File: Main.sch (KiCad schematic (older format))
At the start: 41 parts, among them J1 USB_A FEMALE, J2 USB_A MALE, SW1 SW_Push, SW2 SW_Push, SW3 SW_Push, U1 LTC6995-1, U2 MSP430F5529IPN, U3 TPS2557, U4 TPS2557, U5 TPS2557, U6 TPS2557

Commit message: Addded first portion of battery heater. Contains the temperature sensor and resistive heater. Need to add logic if it will be driven by OBC.
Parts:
- CC1, CC2, CC3, CC4: symbol 2019-06-26_20-23-01:LTC2942CDCB-TRMPBF -> Main-rescue:LTC2942CDCB-TRMPBF-2019-06-26_20-23-01
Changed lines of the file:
@@
 EESchema Schematic File Version 4
 LIBS:Main-cache
-EELAYER 29 0
+EELAYER 26 0
 EELAYER END
 $Descr A2 23386 16535
 encoding utf-8
-Sheet 1 36
+Sheet 1 37
 Title "Electrical Power System"
 Date "2019-04-25"
@@
 	6450 3250 6450 3650
 $Comp
-L 2019-06-26_20-23-01:LTC2942CDCB-TRMPBF CC1
+L Main-rescue:LTC2942CDCB-TRMPBF-2019-06-26_20-23-01 CC1
 U 1 1 5D1F267D
 P 9300 5950
@@
 $EndComp
 $Comp
-L 2019-06-26_20-23-01:LTC2942CDCB-TRMPBF CC2
+L Main-rescue:LTC2942CDCB-TRMPBF-2019-06-26_20-23-01 CC2
 U 1 1 5D20202F
 P 9300 7050
@@
 $EndComp
 $Comp
-L 2019-06-26_20-23-01:LTC2942CDCB-TRMPBF CC3
+L Main-rescue:LTC2942CDCB-TRMPBF-2019-06-26_20-23-01 CC3
 U 1 1 5D20BC4B
 P 9300 8200
@@
 $EndComp
 $Comp
-L 2019-06-26_20-23-01:LTC2942CDCB-TRMPBF CC4
+L Main-rescue:LTC2942CDCB-TRMPBF-2019-06-26_20-23-01 CC4
 U 1 1 5D2149C4
 P 9300 9400
@@
 Text GLabel 11300 9700 2    43   Input ~ 0
 MSP_46_SDA
+$Sheet
+S 8900 12600 500  150
+U 5D20C8DB
+F0 "Battery Heater" 50
+F1 "batteryHeater.sch" 50
+$EndSheet
 $EndSCHEMATC

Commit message: Revisions to battery charge and discharge control. SPV1040 now regulates to 4.2V.
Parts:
- removed CC1, CC2, CC3, CC4: LTC2942, DFN-6_DCB, symbol Main-rescue:LTC2942CDCB-TRMPBF-2019-06-26_20-23-01
- removed J1: USB_A FEMALE, symbol Main-rescue:USB_A-Connector
- removed J2: USB_A MALE, symbol Main-rescue:Conn_01x02-Connector_Generic
- removed PS1: HS-40012, Converter_ACDC:Converter_ACDC_Hahn_HS-400xx_THT, symbol Main-rescue:HS-40012-Converter_ACDC
- removed R1: TBD, symbol Main-rescue:R_Shunt-Device
- removed TH1: 10k, symbol Main-rescue:Thermistor_NTC-Device
- added C? (x2): 0.22u, symbol Device:C
- added C? (x2): 0.1u, symbol Device:C
- added C?: 10u, symbol Device:C
- added D? (x2): D_Schottky, symbol Device:D_Schottky
- added R?: 10m, symbol Main-rescue:R-Device
- added R? (x2): 100k, symbol Device:R
- added R? (x2): R, symbol Device:R
- added U? (x2): TPS2557, symbol Main-rescue:TPS2557
- added U?: LTC2942, symbol Main-rescue:LTC2942
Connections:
- net GNDD: now also C?.2, C?.2, C?.2, C?.2, C?.2, R?.2, R?.2, U?.1 (GND), U?.1 (GND), U?.2 (GND)
- net BDR/5V renamed MPB
- net MPB: now also C?.1, D?.1 (K), U?.2 (IN), U?.3 (IN)
- net Cell1/Cell- renamed PACK+
- net PACK+: now also C?.1, D?.1 (K), R?.1, U?.1 (SENSE+), U?.2 (IN), U?.3 (IN)
- new net: C?.1, R?.1, U?.4 (EN), U?.8 (FAULT!)
- new net: R?.1, U?.5 (ILIM) (x2)
- new net: C?.1, D?.2 (A), D?.2 (A), U?.6 (OUT), U?.6 (OUT), U?.7 (OUT), U?.7 (OUT)
- new net: C?.1, R?.2, U?.4 (EN), U?.8 (FAULT!)
- new net AL!CC: U?.5 (AL!/CC)
- new net Cell1/Cell+: R?.2, U?.6 (SENSE-)
- new net ChargeEnable: R?.1
- new net DischargeEnable: R?.2
- new net SCL: U?.3 (SCL)
- new net SDA: U?.4 (SDA)
- no-connect marks 12 -> 10
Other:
- note added: "Main Power Bus"
- note added: "Rsense = 50mV / Imax\nTake Imax = 5A"
- note added: "to loads"
- note removed: "External Charger"
- note removed: "External Charging Circuit\n"
- note removed: "Thermistor"
- note removed: "This diode prevents the BDR from powering the BCR"
- moved on the sheet: C1, C2, C3, C4, C5, C6, C7, C8, R10, R11, R12, R13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

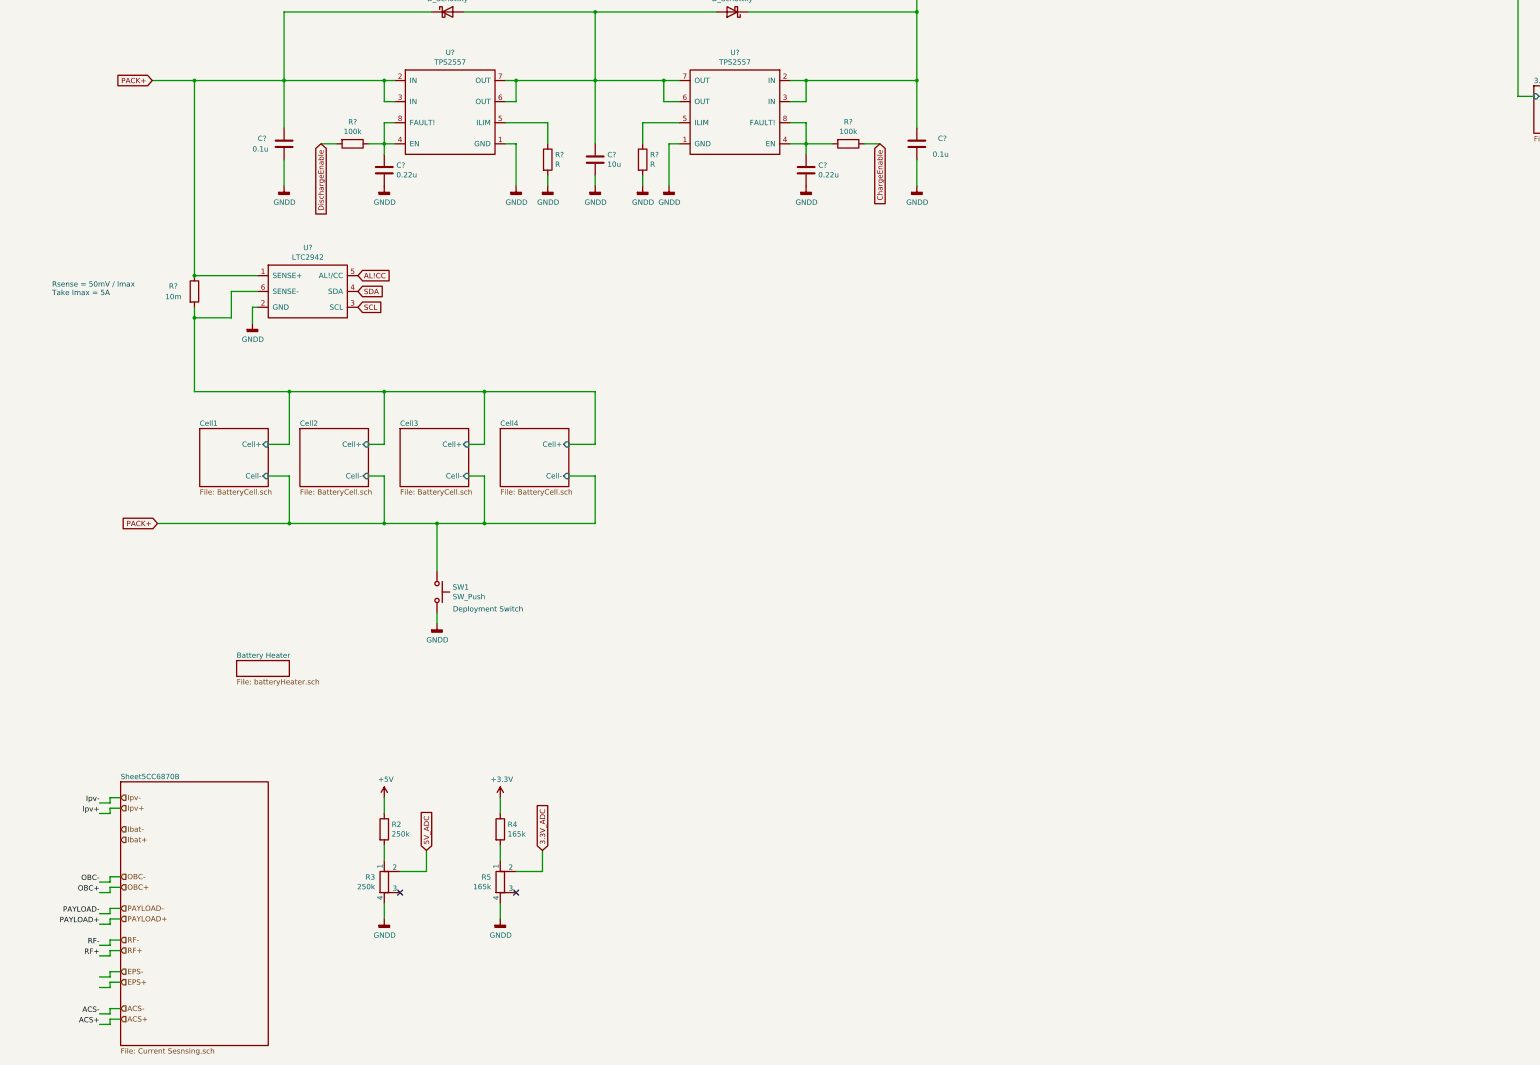
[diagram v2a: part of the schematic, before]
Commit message: Added control circuitry for charge and discharge.
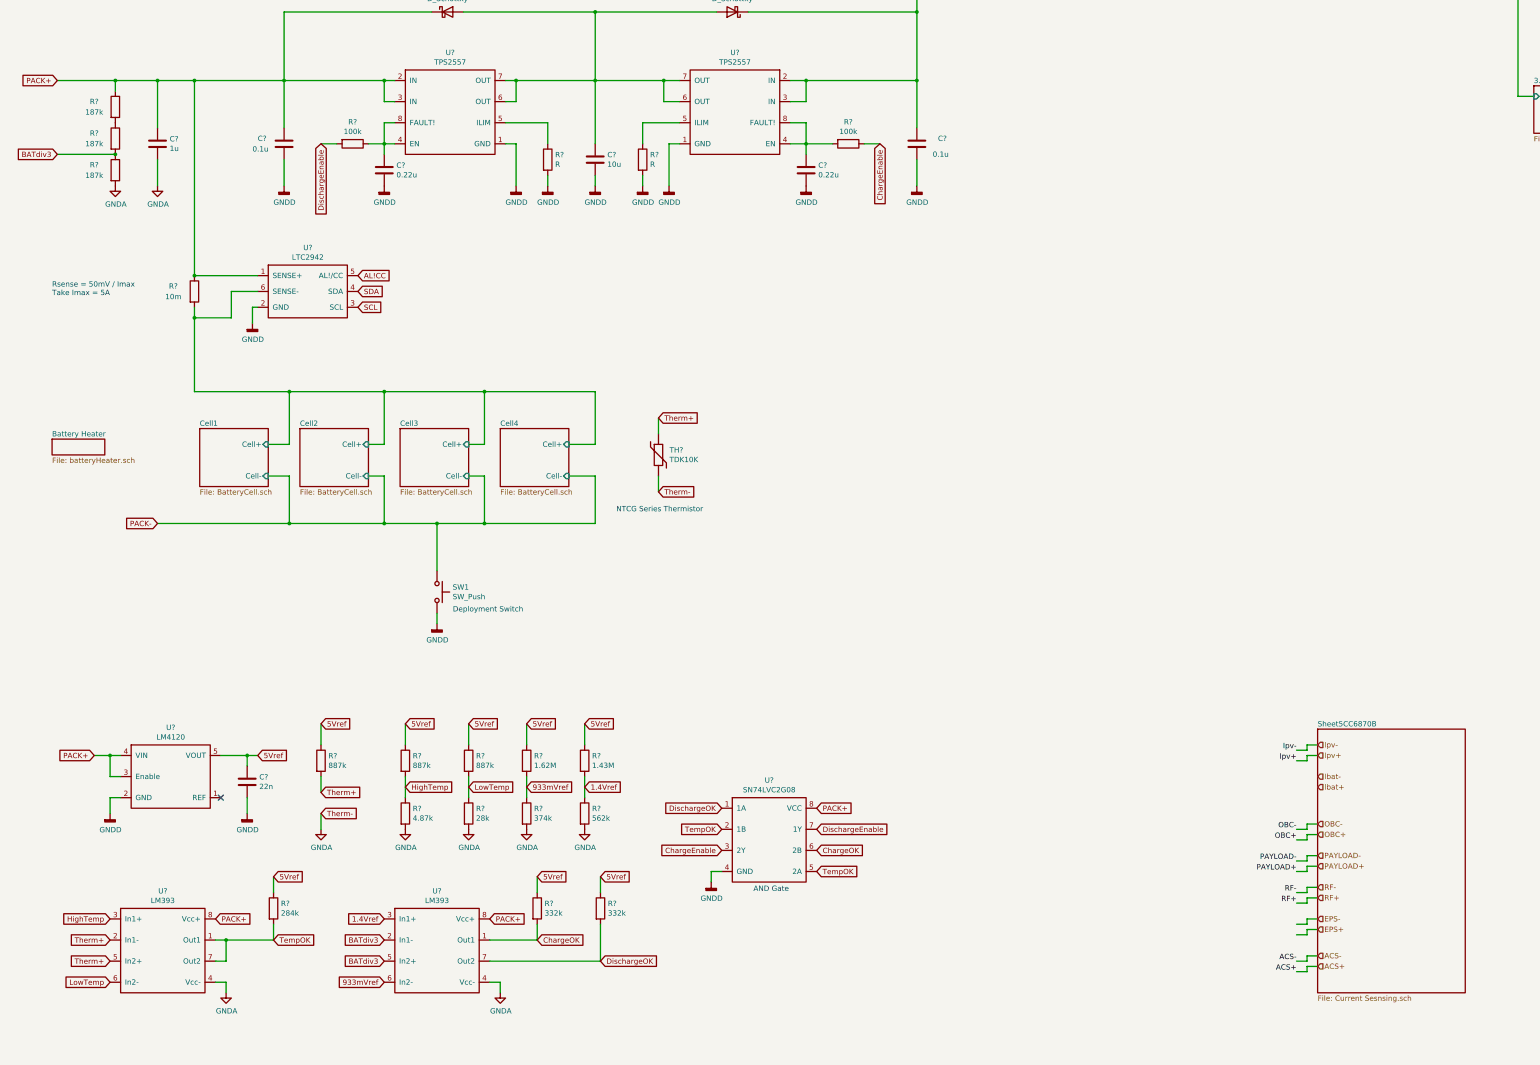
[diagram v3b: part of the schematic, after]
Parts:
- removed R2: 250k, symbol Main-rescue:R-Device
- removed R3: 250k, symbol Main-rescue:R_Shunt-Device
- removed R4: 165k, symbol Main-rescue:R-Device
- removed R5: 165k, symbol Main-rescue:R_Shunt-Device
- added C?: 22n, symbol Device:C
- added C?: 1u, symbol Device:C
- added R? (x3): 887k, symbol Device:R
- added R?: 4.87k, symbol Device:R
- added R?: 28k, symbol Device:R
- added R? (x3): 187k, symbol Main-rescue:R-Device
- added R?: 1.62M, symbol Device:R
- added R?: 374k, symbol Device:R
- added R?: 1.43M, symbol Device:R
- added R?: 562k, symbol Device:R
- added R?: 284k, symbol Device:R
- added R? (x2): 332k, symbol Device:R
- added TH?: TDK10K, symbol Device:Thermistor
- added U?: LM4120, symbol Main-rescue:LM4120
- added U? (x2): LM393, symbol Main-rescue:LM393
- added U?: SN74LVC2G08, symbol Main-rescue:SN74LVC2G08
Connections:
- net ChargeEnable: now also U?.3 (2Y)
- net DischargeEnable: now also U?.7 (1Y)
- net GNDD: now also C?.2, U?.2 (GND), U?.4 (GND)
- net PACK+: now also C?.1, R?.1, U?.3 (Enable), U?.4 (VIN), U?.8 (VCC), U?.8 (Vcc+), U?.8 (Vcc+); no longer SW1.1
- new net: R?.1, R?.2
- new net 1.4Vref: R?.1, R?.2, U?.3 (In1+)
- new net 5Vref: C?.1, R?.1, R?.1, R?.1, R?.1, R?.1, R?.1, R?.1, R?.1, U?.5 (VOUT)
- new net 933mVref: R?.1, R?.2, U?.6 (In2-)
- new net BATdiv3: R?.1, R?.2, U?.2 (In1-), U?.5 (In2+)
- new net ChargeOK: R?.2, U?.1 (Out1), U?.6 (2B)
- new net DischargeOK: R?.2, U?.1 (1A), U?.7 (Out2)
- new net GNDA: C?.2, R?.2, R?.2, R?.2, R?.2, R?.2, TH?.2, U?.4 (Vcc-), U?.4 (Vcc-)
- new net HighTemp: R?.1, R?.2, U?.3 (In1+)
- new net LowTemp: R?.1, R?.2, U?.6 (In2-)
- new net PACK-: SW1.1
- new net TempOK: R?.2, U?.1 (Out1), U?.2 (1B), U?.5 (2A), U?.7 (Out2)
- new net Therm+: R?.2, TH?.1, U?.2 (In1-), U?.5 (In2+)
- no-connect marks 10 -> 9
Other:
- note added: "AND Gate"
- note added: "NTCG Series Thermistor"

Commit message: Each deployment switch is now electrically coupled with a FET. The system switch is now a FET.
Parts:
- removed R6: 86.6k, symbol Main-rescue:R-Device
- removed R7: 1M, symbol Main-rescue:R-Device
- removed R8: 887k, symbol Main-rescue:R-Device
- removed SW2, SW3: SW_Push, symbol Main-rescue:SW_Push-Switch
- removed U1: LTC6995-1, symbol Main-rescue:LTC6995-1-CustomSymbols
- added M? (x2): MNMOS, symbol pspice:MNMOS
- added M? (x3): MPMOS-pspice, symbol Main-rescue:MPMOS-pspice
- added R? (x5): 100k, symbol Device:R
- added R?: 1M, symbol Main-rescue:R-Device
- added R?: 887k, symbol Main-rescue:R-Device
- added R?: 86.6k, symbol Main-rescue:R-Device
- added SW? (x2): SW_Push, symbol Main-rescue:SW_Push-Switch
- added U?: LTC6995-1, symbol Main-rescue:LTC6995-1
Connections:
- net +5V: now also M?.1 (D)
- net GNDD: now also M?.3 (S), M?.3 (S), R?.2, R?.2, R?.2, SW?.1, SW?.1, U?.1 (RST), U?.2 (GND); no longer SW1.2
- net MPB: now also M?.3 (S), R?.1
- net PACK+: now also SW1.1
- net PACK-: now also M?.1 (D); no longer SW1.1
- new net: M?.2 (G), R?.1, SW1.2
- new net: M?.1 (D), M?.3 (S), R?.1
- new net: M?.2 (G), R?.2, SW?.2 (x2)
- new net: M?.1 (D), M?.3 (S), R?.1, R?.1, U?.5 (V+)
- new net: M?.1 (D), M?.2 (G), R?.2
- new net: R?.2, U?.3 (SET)
- new net: R?.1, R?.2, U?.4 (DIV)
- new net: M?.2 (G), R?.1, R?.1, U?.6 (OUT)
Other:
- note added: "30 Minute Timer"
- note added: "Deployment Switch 1"
- note added: "Deployment\nSwitch 2"
- note added: "Deployment\nSwitch 3"
- note added: "Inhibit Switch 1"
- note added: "Inhibit\nSwitch 2"
- note added: "Inhibit\nSwitch 3"
- note added: "System Switch"
- note removed: "86.6k resistor sets timer length to 31 minutes.\nLow tolerance required."
- note removed: "Deployment Switch"
- note removed: "Main Power Bus"
- note removed: "R_total = 25 mOhm"
- note removed: "to loads"
- moved on the sheet: C1, C2, C3, C4, C5, C6, C7, C8, R10, R11, R12, R13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

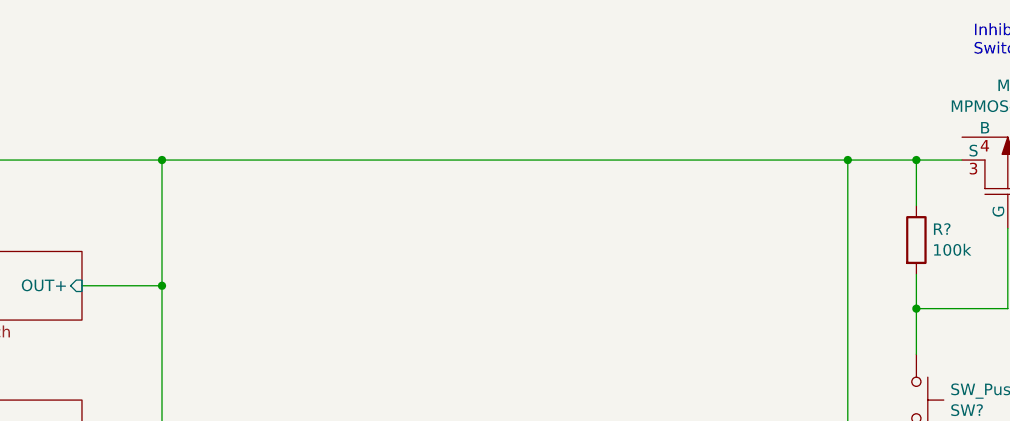
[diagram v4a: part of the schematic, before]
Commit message: added sense resistor for solar cells
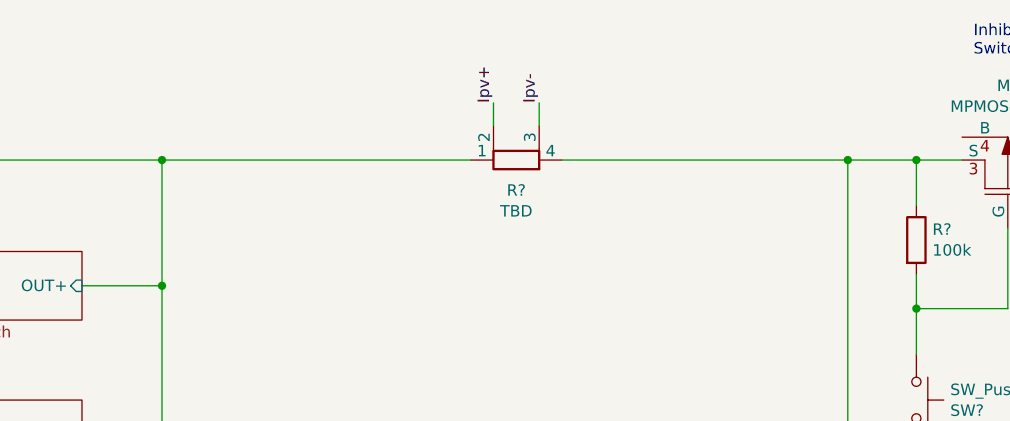
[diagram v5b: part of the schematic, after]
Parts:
- added R?: TBD, symbol Main-rescue:R_Shunt-Device
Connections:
- net Ipv+: now also R?.2
- net Ipv-: now also R?.3
- net MPB: now also R?.1; no longer C?.1, D?.1 (K), M?.3 (S), R?.1, U?.2 (IN), U?.3 (IN)
- new net: C?.1, D?.1 (K), M?.3 (S), R?.1, R?.4, U?.2 (IN), U?.3 (IN)
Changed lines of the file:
@@
 Wire Wire Line
 	2100 7300 2100 7050
-Connection ~ 6300 2150
 Connection ~ 9300 5650
 Wire Wire Line
 	9300 2150 9300 5650
-Wire Wire Line
-	6300 2150 9300 2150
 $Comp
 L pspice:MNMOS M?
@@
 Wire Wire Line
 	9300 2150 9600 2150
-Connection ~ 9300 2150
 $Comp
 L Device:R R?
@@
 Text Notes 12250 2700 0    50   ~ 0
 30 Minute Timer
+Wire Wire Line
+	7950 2000 7950 1900
+Wire Wire Line
+	7750 2000 7750 1900
+$Comp
+L Main-rescue:R_Shunt-Device R?
+U 1 1 5E5897E1
+P 7850 2150
+F 0 "R?" V 7717 2150 50  0000 C CNN
+F 1 "TBD" V 7626 2150 50  0000 C CNN
+F 2 "" V 7780 2150 50  0001 C CNN
+F 3 "~" H 7850 2150 50  0001 C CNN
+	1    7850 2150
+	0    -1   -1   0
+$EndComp
+Text Label 7950 1900 1    50   ~ 0
+Ipv-
+Text Label 7750 1900 1    50   ~ 0
+Ipv+
+Wire Wire Line
+	6300 2150 7650 2150
+Connection ~ 6300 2150
+Wire Wire Line
+	8050 2150 9300 2150
+Connection ~ 9300 2150
 $EndSCHEMATC

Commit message: added RBF pin
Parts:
- added SW?: RBF Mechanism, symbol Main-rescue:SW_Push-Switch
- added U? (x7): MAX44284E, symbol MAX44284E:MAX44284E
- SW1: value SW_Push -> Deployment Switch 1
- SW?: value SW_Push -> Deployment Switch 2
- SW?: value SW_Push -> Deployment Switch 3
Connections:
- net +5V: now also U?.1 (Vdd), U?.1 (Vdd), U?.1 (Vdd), U?.1 (Vdd), U?.1 (Vdd), U?.1 (Vdd), U?.1 (Vdd)
- net ACS+: now also U?.3 (RS+)
- net ACS-: now also U?.6 (RS-)
- net EPS+: now also U?.3 (RS+)
- net EPS-: now also U?.6 (RS-)
- net GNDD: now also U?.2 (GND), U?.2 (GND), U?.2 (GND), U?.2 (GND), U?.2 (GND), U?.2 (GND), U?.2 (GND)
- net Ibat+: now also U?.3 (RS+)
- net Ibat-: now also U?.6 (RS-)
- net Ipv+: now also U?.3 (RS+)
- net Ipv-: now also U?.6 (RS-)
- net OBC+: now also U?.3 (RS+)
- net OBC-: now also U?.6 (RS-)
- net PAYLOAD+: now also U?.3 (RS+)
- net PAYLOAD-: now also U?.6 (RS-)
- net RF+: now also U?.3 (RS+)
- net RF-: now also U?.6 (RS-)
- net at M?.2 (G), R?.2: now also M?.2 (G), R?.2, SW?.2; no longer SW?.2
- new net: SW?.1, SW?.2, SW?.2
- new net ACS_ADC: U?.5 (OUT)
- new net EPS_ADC: U?.5 (OUT)
- new net Ibat_ADC: U?.5 (OUT)
- new net Ipv_ADC: U?.5 (OUT)
- new net OBC_ADC: U?.5 (OUT)
- new net PAYLOAD_ADC: U?.5 (OUT)
- new net RF_ADC: U?.5 (OUT)
- new net ~ACS_SHDN: U?.4 (~SHDN)
- new net ~EPS_SHDN: U?.4 (~SHDN)
- new net ~Ibat_SHDN: U?.4 (~SHDN)
- new net ~Ipv_SHDN: U?.4 (~SHDN)
- new net ~OBC_SHDN: U?.4 (~SHDN)
- new net ~PAYLOAD_SHDN: U?.4 (~SHDN)
- new net ~RF_SHDN: U?.4 (~SHDN)
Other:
- note added: "mom-off"
- note removed: "Deployment\nSwitch 2"
- note removed: "Deployment\nSwitch 3"
- note removed: "Inhibit Switch 1"
- moved on the sheet: C?, R?, SW?, U2, U?

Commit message: prog
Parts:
- removed M?: MPMOS-pspice, symbol Main-rescue:MPMOS-pspice
- removed R?: 100k, symbol Device:R
- removed SW?: RBF Mechanism, symbol Main-rescue:SW_Push-Switch
- added C? (x2): 13uF, symbol Main-rescue:C-Device
- added L?: 373uH, symbol Main-rescue:L-Device
- added M?: MPMOS, symbol pspice:MPMOS
- added R?: 100k, symbol Main-rescue:R-Device
- added R?: 100k, symbol Device:R
- added U?: LM5165Y, Package_SON:Texas_S-PVSON-N10_ThermalVias, symbol Main-rescue:LM5165Y-Regulator_Switching
- SW1: value Deployment Switch 1 -> RBF Pin
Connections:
- net +5V: now also C?.1, U?.2 (VIN)
- net GNDD: now also C?.2, C?.2, R?.1, U?.10 (GND), U?.5 (RT), U?.9 (HYS)
- net PACK+: no longer SW1.1
- net GroundInhibitSignal: now reaches M?.2 (G), SW1.2
- net at C?.1, D?.1 (K), R?.4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: no longer M?.3 (S), R?.1
- net at M?.2 (G), R?.2: now also SW?.2; no longer M?.2 (G), R?.2
- net at SW?.2: now also M?.2 (G), R?.2; no longer SW?.2
- net at M?.1 (D), R?.1, R?.1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: now also M?.3 (S)
- net at M?.1 (D), R?.2: now also M?.2 (G)
- new net: R?.2, SW1.1
- new net: L?.1, U?.1 (SW)
- new net: R?.2, U?.3 (ILIM)
- new net: C?.1, L?.2, U?.8 (VOUT)
- new net UnregulatedPreInhibit: M?.3 (S), R?.1
- new net VoltageRegulatorInput: M?.1 (D)
- no-connect marks 9 -> 10
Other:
- note added: "Battery Pack, Battery protection, Charge/Discharge Load Switches and \nSolar Cells with MPPT"
- note added: "Charge/Discharge Logic"
- note added: "Inhibit Switches, RBF pin and 30 minute timer"
- note added: "Inhibit \nSwitch 1"
- note added: "Load Switches"
- note added: "NTCG Series \nThermistor"
- note added: "Voltage Regulators"
- note removed: "Deployment Switch 1"
- note removed: "NTCG Series Thermistor"
- moved on the sheet: C1, C2, C3, C4, C5, C6, C7, C8, C?, D?, M?, R10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

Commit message: finish
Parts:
- removed R?: 100k, symbol Device:R
- removed SW1: RBF Pin, symbol Main-rescue:SW_Push-Switch
- added C? (x4): 0.1u, symbol Main-rescue:C-Device
- added C? (x4): 150u, symbol Main-rescue:C-Device
- added R?: 100k, symbol Device:R
- added R? (x4): R, symbol Main-rescue:R-Device
- added R? (x4): TBD, symbol Main-rescue:R_Shunt-Device
- added SW?: Deployment Switch 1, symbol Main-rescue:SW_Push-Switch
- added SW?: RBF Pin, symbol Main-rescue:SW_Push-Switch
- added U? (x4): TPS2557, symbol Main-rescue:TPS2557-CustomSymbols
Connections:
- net ACS: now also C?.1, U?.7 (OUT)
- net ACS+: now also R?.2
- net ACS-: now also R?.3
- net GNDD: now also C?.2, C?.2, C?.2, C?.2, C?.2, C?.2, C?.2, C?.2, R?.2, R?.2, R?.2, R?.2, SW?.2, U?.1 (GND), U?.1 (GND), U?.1 (GND), U?.1 (GND); no longer SW?.1
- net OBC: now also C?.1, U?.7 (OUT)
- net OBC+: now also R?.2
- net OBC-: now also R?.3
- net PACK+: now also SW?.1
- net PAYLOAD: now also C?.1, U?.7 (OUT)
- net PAYLOAD+: now also R?.2
- net PAYLOAD-: now also R?.3
- net RF: now also C?.1, U?.7 (OUT)
- net RF+: now also R?.2
- net RF-: now also R?.3
- net +3V3: now reaches C?.1, L?.2, U?.8 (VOUT)
- net +3V3: now also R?.1, R?.1, R?.1, R?.1
- net GroundInhibitSignal renamed InhibitSwitch1
- net InhibitSwitch1: now also R?.1, SW?.2
- new net: R?.2, SW?.1, SW?.1
- new net: C?.1, R?.4, U?.2 (IN) (x4)
- new net: R?.1, U?.5 (ILIM) (x4)
- no-connect marks 10 -> 18
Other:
- note added: "Battery Heater"
- note added: "Coulomb counter"
- note added: "Current Sensing Op Amps"
- note added: "Inhibit Switch 1"
- note added: "RBF Mechanism\nmom-off \n(when pin is in switch is open)"
- note added: "Roller Switch\nmom-off"
- note added: "Tactical Switch\nmom-off"
- note removed: "Inhibit \nSwitch 1"
- note removed: "mom-off"
- moved on the sheet: C1, C2, C3, C4, C5, C6, C7, C8, C?, L?, M?, R10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
